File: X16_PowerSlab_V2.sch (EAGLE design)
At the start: 33 parts, among them J1 CONN_796636-3, J2 CONN_796636-3, J3 CONN_ET60T, U1 LINEAR_AZ1117CR-3.3TRG1DIODES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

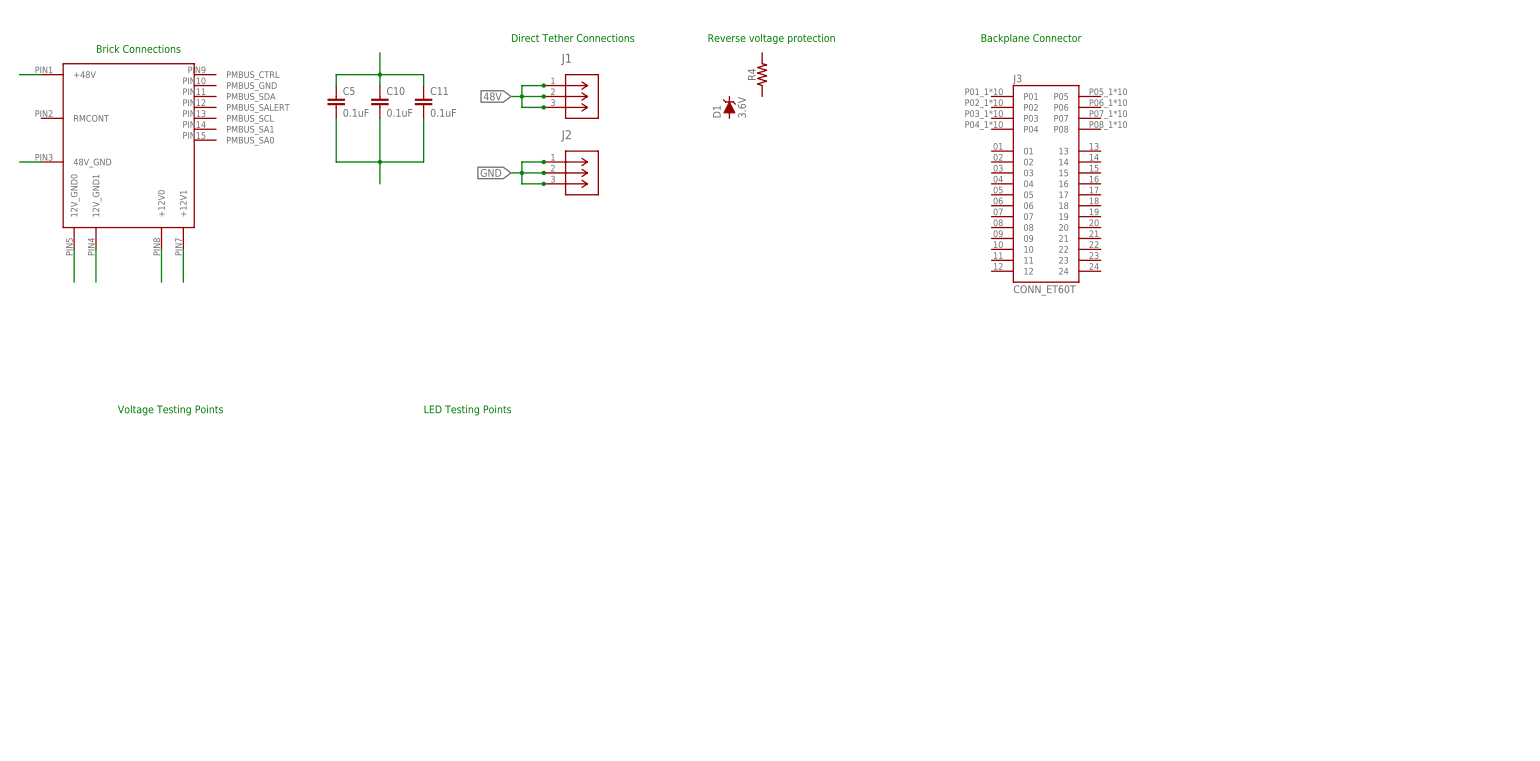
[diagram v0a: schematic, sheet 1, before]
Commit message: Updated reverse voltage protection
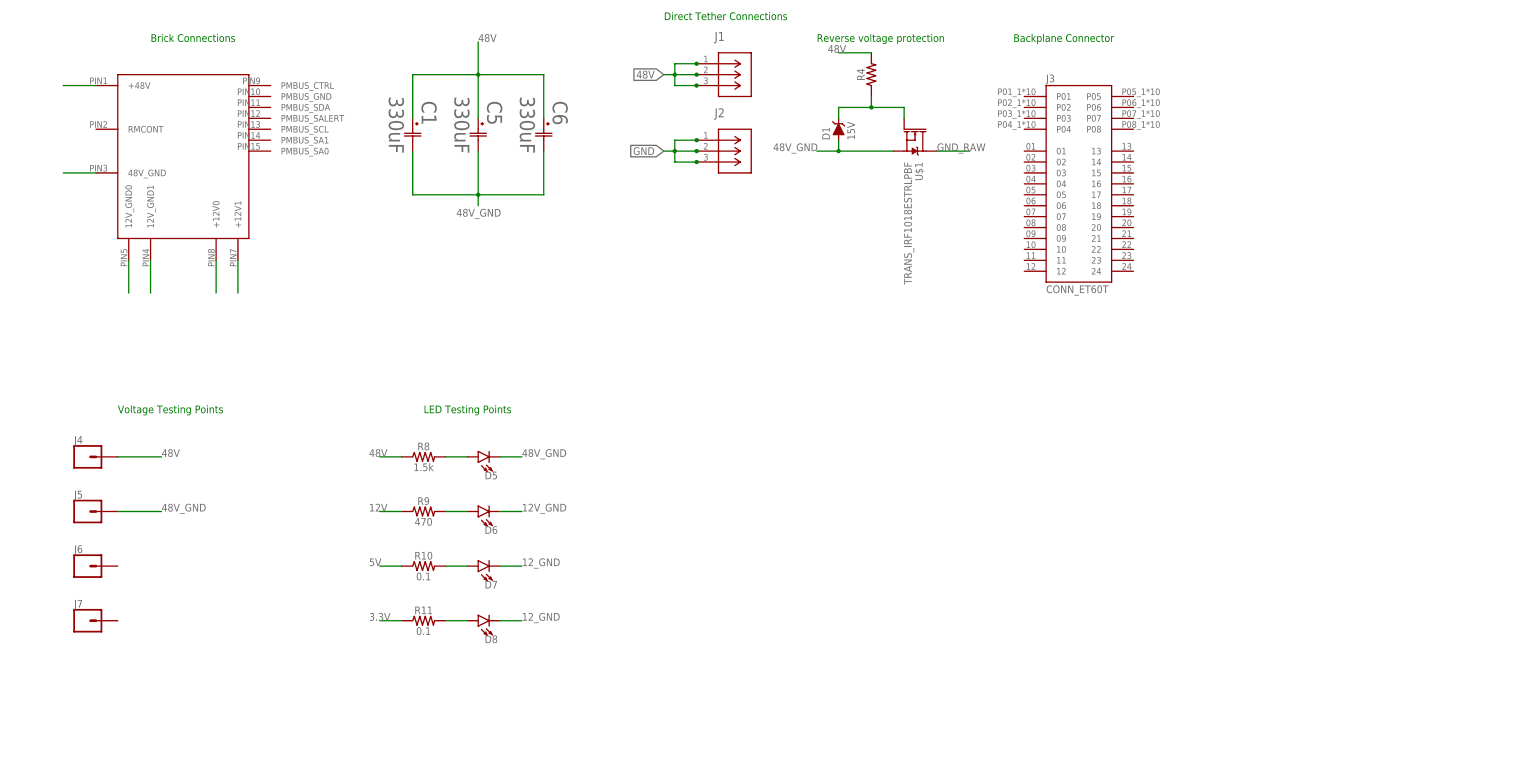
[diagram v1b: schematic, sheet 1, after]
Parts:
- removed C10, C11: 0.1uF, SparkFun-Capacitors:0.1UF-0603-25V-(+80/-20%)
- added C1, C6: 330uF, X15_Brickstribution:CAP_MAL215099112E3CAP_099112E3_VIS-M
- added D5, D6, D7, D8: (no value), SparkFun-LED:LED0603
- added J4, J5, J6, J7: (no value), SparkFun-Connectors:CONN_01
- added R10, R11: 0.1, SparkFun-Resistors:0.1OHM-0603-1/3W-1%
- added R8: 1.5k, SparkFun-Resistors:0.1OHM-0603-1/3W-1%
- added R9: 470, SparkFun-Resistors:0.1OHM-0603-1/3W-1%
- added U$6: CONN_BMR480_BRICK, X16_Power_Slab:CONN_BMR480_BRICK
- C5: value 0.1uF -> 330uF; device SparkFun-Capacitors:0.1UF-0603-25V-(+80/-20%) -> X15_Brickstribution:CAP_MAL215099112E3CAP_099112E3_VIS-M
- D1: value 3.6V -> 15V
- R1: value 1k -> (none)
- R2: value 3.32k -> (none)
- R3: value 12.4k -> (none)
- R5: value 600 -> (none)
- R6: value 300 -> (none)
- R7: value 200 -> (none)
- U$1: value CONN_BMR480_BRICK -> TRANS_IRF1018ESTRLPBF; device X16_Power_Slab:CONN_BMR480_BRICK -> X15_Brickstribution:TRANS_IRF1018ESTRLPBF
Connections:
- removed net N$15: U$1.+48V
- removed net N$16: C10.1, C11.1, C5.1
- removed net N$17: C10.2, C11.2, C5.2
- new net 12V: R9.1
- new net 12V_GND: D6.C
- new net 12_GND: D7.C, D8.C
- new net 3.3V: R11.1
- new net 48V_GND: C1.2, C5.2, C6.2, D1.A, D5.C, J5.1, U$1.S
- new net 5V: R10.1
- new net GND_RAW: U$1.D
- new net N$19: U$6.12V_GND1
- new net N$20: U$6.+12V0
- new net N$21: U$6.+12V1
- new net N$22: U$6.48V_GND
- new net N$7: D1.C, R4.1, U$1.G
- new net N$9: D5.A, R8.2
- net 48V: now also C1.1, C5.1, C6.1, J4.1, R4.2, R8.1
- net N$10: now also D6.A, R9.2; no longer U$1.12V_GND0
- net N$11: now also D7.A, R10.2; no longer U$1.12V_GND1
- net N$12: now also D8.A, R11.2; no longer U$1.+12V0
- net N$13: now also U$6.+48V; no longer U$1.+12V1
- net N$14: now also U$6.12V_GND0; no longer U$1.48V_GND
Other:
- moved on the sheet: C2, C3, C4, CIN1, CIN2, COUT1, COUT2, COUT3, D1, D2, D3, D4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

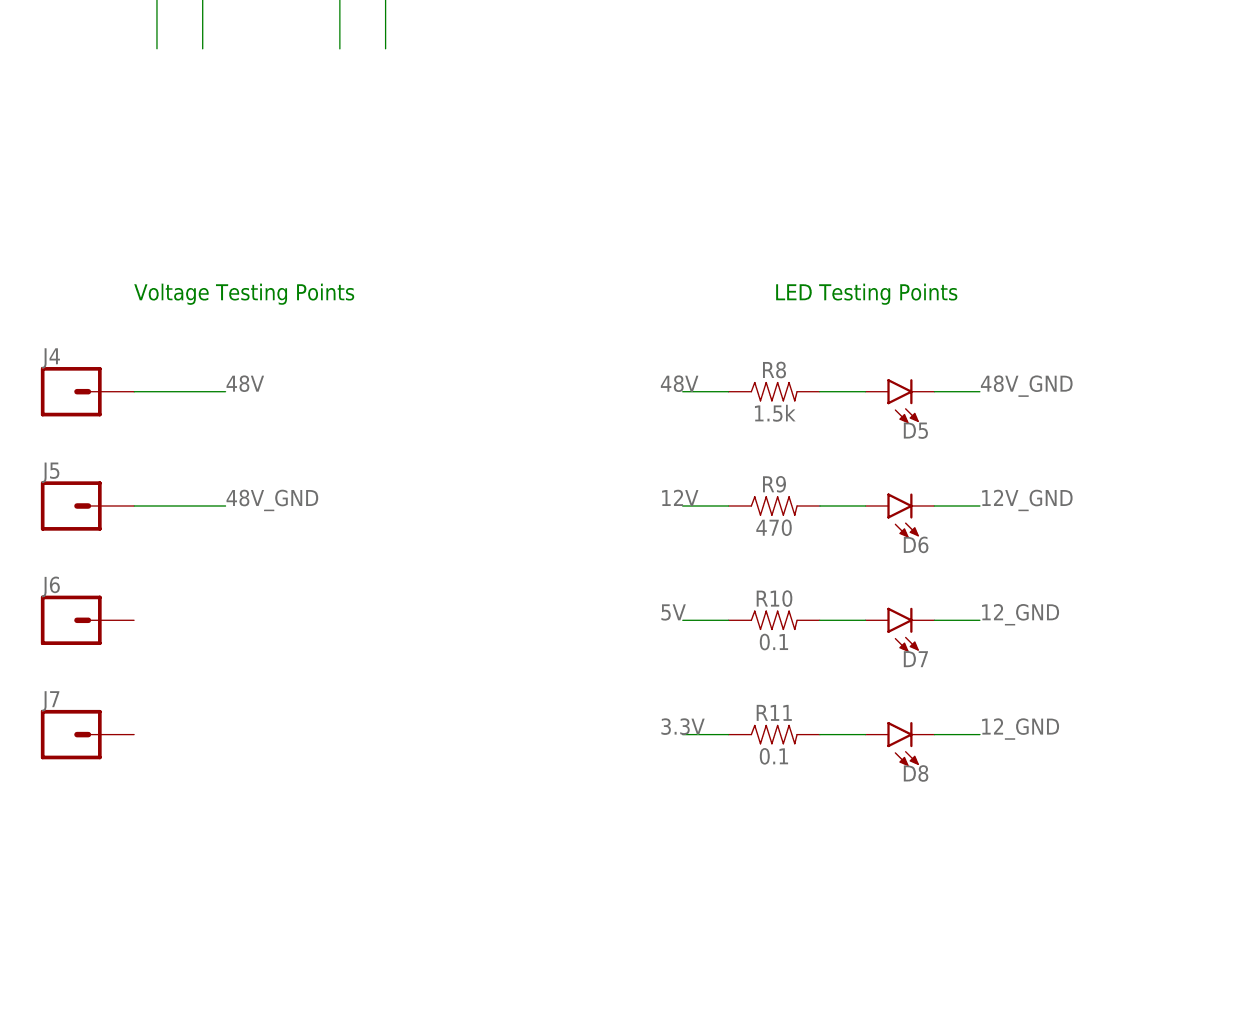
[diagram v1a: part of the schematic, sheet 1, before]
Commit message: Added testpoints, fixed some errors with values
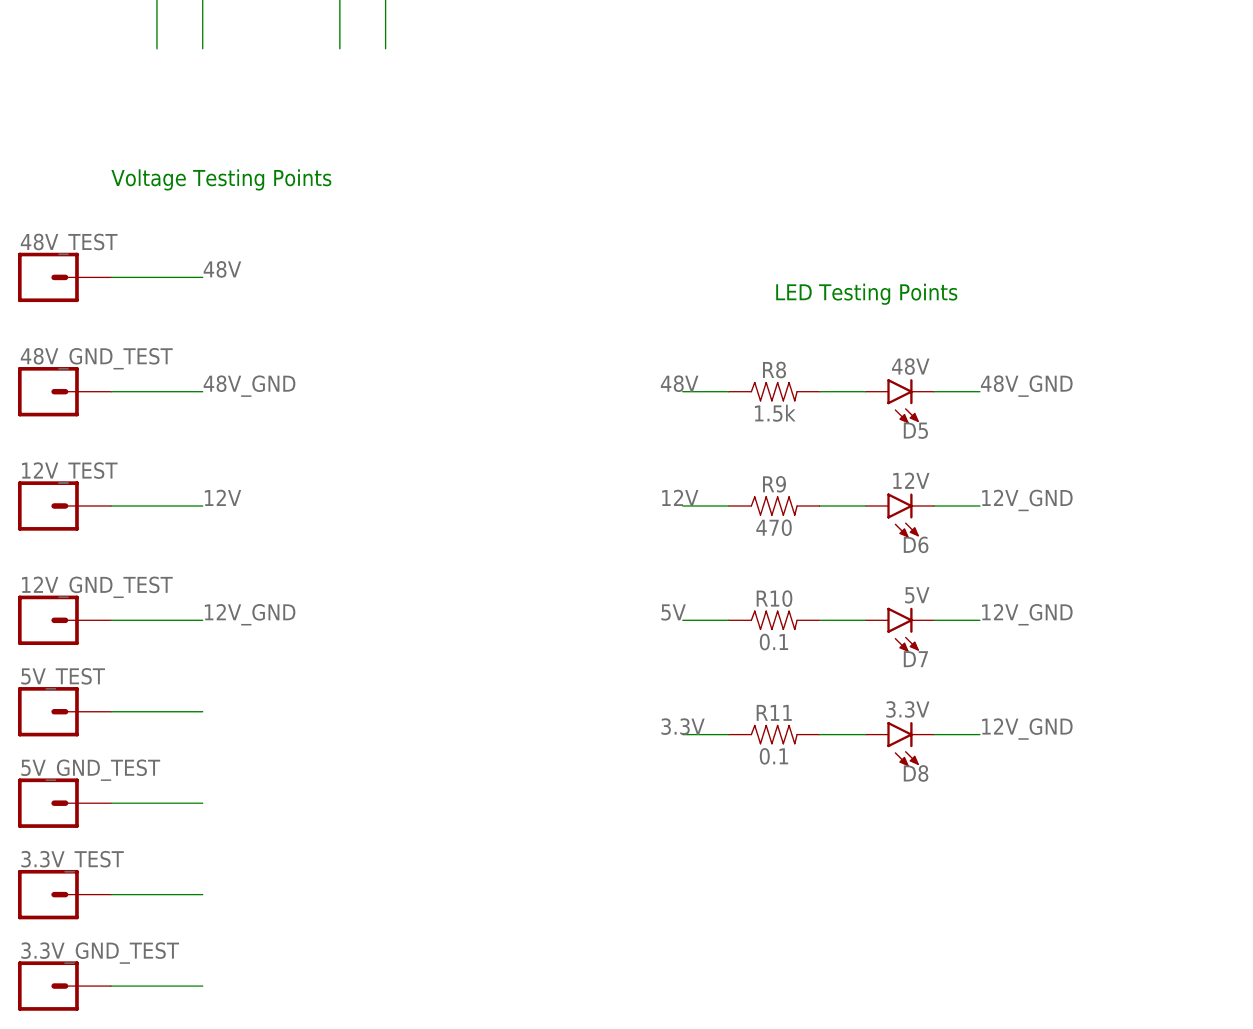
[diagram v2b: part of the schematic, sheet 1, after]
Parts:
- removed J4, J5, J6, J7: (no value), SparkFun-Connectors:CONN_01
- added 12V_GND_TEST, 12V_TEST, 3.3V_GND_TEST, 3.3V_TEST, 48V_GND_TEST, 48V_TEST, 5V_GND_TEST, 5V_TEST: (no value), SparkFun-Connectors:CONN_01
- D5: value (none) -> 48V
- D6: value (none) -> 12V
- D7: value (none) -> 5V
- D8: value (none) -> 3.3V
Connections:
- removed net 12_GND: D7.C, D8.C
- new net N$15: 5V_TEST.1
- new net N$16: 5V_GND_TEST.1
- new net N$17: 3.3V_TEST.1
- new net N$18: 3.3V_GND_TEST.1
- net 12V: now also 12V_TEST.1
- net 12V_GND: now also 12V_GND_TEST.1, D7.C, D8.C
- net 48V: now also 48V_TEST.1; no longer J4.1
- net 48V_GND: now also 48V_GND_TEST.1; no longer J5.1

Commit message: schematic finished
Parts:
- removed 3.3V_GND_TEST, 3.3V_TEST: (no value), SparkFun-Connectors:CONN_01
- removed C3: 10uF, SparkFun-Capacitors:0.1UF-0603-25V-(+80/-20%)
- removed C4: 22uF, SparkFun-Capacitors:0.1UF-0603-25V-(+80/-20%)
- removed D4, D8: 3.3V, SparkFun-LED:LED0603
- removed R11: 0.1, SparkFun-Resistors:0.1OHM-0603-1/3W-1%
- removed R7: (no value), SparkFun-Resistors:RESISTOR0603
- removed U$6: CONN_BMR480_BRICK, X16_Power_Slab:CONN_BMR480_BRICK
- removed U1: LINEAR_AZ1117CR-3.3TRG1DIODES_AZ1117CH-3.3TRG1_0_0, X16_Power_Slab:LINEAR_AZ1117CR-3.3TRG1DIODES_AZ1117CH-3.3TRG1_0_0
- U$3: value 3.3V_TESTPOINT -> CONN_BMR480_BRICK; device X15-Conversion-Parts-Library:3.3V_TESTPOINT -> X16_Power_Slab:CONN_BMR480_BRICK
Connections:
- removed net 12V/1.1B: R5.1, U$5.12V
- removed net 12V/2.1A: CIN1.+, CIN2.1, U$2.VIN
- removed net 3.3V: R11.1
- removed net 3.3V/1.4C: R7.1, U$3.3.3V
- removed net 3.3V/2.1B: C4.1, U1.OUPUT
- removed net 5.2V/1.5B: R6.1, U$4.5.2V
- removed net 5.2V/2.1A: C3.1, COUT1.+, COUT2.+, COUT3.+, L1.2, R2.2, U1.INPUT
- removed net GND/1.5A: D2.C, D3.C, D4.C
- removed net GND/2.2D: C3.2, C4.2, CIN1.-, CIN2.2, COUT1.-, COUT2.-, COUT3.-, DIODE.2, R3.1, U$2.GND, U1.GND
- removed net N$12: D8.A, R11.2
- removed net N$13: U$6.+48V
- removed net N$14: U$6.12V_GND0
- removed net N$15: 5V_TEST.1
- removed net N$16: 5V_GND_TEST.1
- removed net N$17: 3.3V_TEST.1
- removed net N$18: 3.3V_GND_TEST.1
- removed net N$19: U$6.12V_GND1
- removed net N$20: U$6.+12V0
- removed net N$21: U$6.+12V1
- removed net N$22: U$6.48V_GND
- removed net N$6: D4.A, R7.2
- new net 5.2V: 5V_TEST.1, COUT1.+, COUT2.+, COUT3.+, L1.2, R2.2, R6.1, U$4.5.2V
- new net PMBUS_CTRL: J3.17, U$3.PMBUS_CTRL
- new net PMBUS_GND: J3.18, U$3.PMBUS_GND
- new net PMBUS_SA0: J3.22, U$3.PMBUS_SA0
- new net PMBUS_SA1: J3.23, U$3.PMBUS_SA1
- new net PMBUS_SALERT: J3.20, U$3.PMBUS_SALERT
- new net PMBUS_SCL: J3.21, U$3.PMBUS_SCL
- new net PMBUS_SDA: J3.19, U$3.PMBUS_SDA
- net 12V: now also CIN1.+, CIN2.1, J3.P01, J3.P02, R5.1, U$2.VIN, U$3.+12V0, U$3.+12V1, U$5.12V
- net 12V_GND: now also J3.P03, J3.P04; no longer 12V_GND_TEST.1, D6.C, D7.C, D8.C
- net 48V: now also U$3.+48V
- net 48V_GND: now also U$3.48V_GND
- net 5V: now also J3.P05, J3.P06
- net GND: now also 12V_GND_TEST.1, 5V_GND_TEST.1, CIN1.-, CIN2.2, COUT1.-, COUT2.-, COUT3.-, D2.C, D3.C, D6.C, D7.C, DIODE.2, J3.P07, J3.P08, R3.1, U$2.GND, U$3.12V_GND0, U$3.12V_GND1; no longer J2.1, J2.2, J2.3
- net GND_RAW: now also J2.1, J2.2, J2.3
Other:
- note removed: "Linear Regulator"
- moved on the sheet: C1, C5, C6, D1, J1, J2, J3, R4, U$1

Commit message: Started placing components on board
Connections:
- removed net 5.2V: 5V_TEST.1, COUT1.+, COUT2.+, COUT3.+, L1.2, R2.2, R6.1, U$4.5.2V
- net 5V: now also 5V_TEST.1, COUT1.+, COUT2.+, COUT3.+, L1.2, R2.2, R6.1, U$4.5.2V
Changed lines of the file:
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@@
 <label x="264.16" y="154.94" size="1.778" layer="95"/>
 </segment>
-</net>
-<net name="5.2V" class="0">
 <segment>
 <pinref part="5V_TEST" gate="J1" pin="1"/>
@@
 </segment>
 </net>
-<net name="5.2V" class="0">
+<net name="5V" class="0">
 <segment>
 <pinref part="L1" gate="G$1" pin="2"/>

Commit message: Started placing board components
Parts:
- removed C1, C5, C6: 330uF, X15_Brickstribution:CAP_MAL215099112E3CAP_099112E3_VIS-M
- added C3, C4, C7: 330uF, SparkFun-Capacitors:10UF-POLAR-0603-6.3V-20%(TANT)
- added CR1: DIODE(Z)_SMBJ5357B-TPDIODE_DO-214AA_4P38X3P62_MCC-M, X15_Brickstribution:DIODE(Z)_SMBJ5357B-TPDIODE_DO-214AA_4P38X3P62_MCC-M
- added D4: 250mA/100V, SparkFun-DiscreteSemi:DIODE-BAS16J
- D7: value 5V -> 5.2V
- R1: value (none) -> 1k
- R10: value 0.1 -> 100
- R2: value (none) -> 3.32k
- R4: value (none) -> 1M
- R5: value (none) -> 600
- R6: value (none) -> 300
- RADJ: value (none) -> 12.4k
- renumbered 5V_GND_TEST to 5.2V_GND_TEST, 5V_TEST to 5.2V_TEST, R3 to RADJ
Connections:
- net 5V renamed 5.2V
- net 12V: now also CR1.1, D4.A, D4.C
- net 48V: now also C3.+, C4.+, C7.+; no longer C1.1, C5.1, C6.1
- net 48V_GND: now also C3.-, C4.-, C7.-; no longer C1.2, C5.2, C6.2
- net GND: now also CR1.2
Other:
- note added: "Back EMF Protection"
- note added: "Reverse Voltage Protection"
